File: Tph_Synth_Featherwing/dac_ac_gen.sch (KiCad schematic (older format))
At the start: 10 parts, among them U4 MCP4728

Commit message: Added BOM and upgraded to kicad 5.0
Signed-off-by: Tisham Dhar <whatnickd@gmail.com>
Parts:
- C13, C14, C15, C16, C17: manf# (none) -> GCM188L81H104KA57D
- R16, R17: manf# (none) -> RC0603FR-072K2L
- TP6, TP7: DNP (none) -> (none)
- U4: manf# (none) -> MCP4728-E/UN
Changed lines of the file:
@@
 EESchema Schematic File Version 4
-LIBS:Tph_Synth_Featherwing-cache
-EELAYER 26 0
+EELAYER 30 0
 EELAYER END
 $Descr A4 11693 8268
@@
 F 2 "Package_SO:MSOP-10_3x3mm_P0.5mm" H 4110 2770 50  0001 C CNN
 F 3 "http://ww1.microchip.com/downloads/en/DeviceDoc/22187E.pdf" H 4110 3620 50  0001 C CNN
+F 4 "MCP4728-E/UN" H 4110 3370 50  0001 C CNN "manf#"
 	1    4110 3370
 	1    0    0    -1
@@
 F 2 "Capacitor_SMD:C_0603_1608Metric" H 4380 3030 50  0001 C CNN
 F 3 "~" H 4380 3030 50  0001 C CNN
+F 4 "GCM188L81H104KA57D" H 4380 3030 50  0001 C CNN "manf#"
 	1    4380 3030
 	0    1    1    0
@@
 F 2 "Resistor_SMD:R_0603_1608Metric" H 3075 3135 50  0001 C CNN
 F 3 "~" H 3075 3135 50  0001 C CNN
+F 4 "RC0603FR-072K2L" H 3075 3135 50  0001 C CNN "manf#"
 	1    3075 3135
 	1    0    0    -1
@@
 F 2 "Resistor_SMD:R_0603_1608Metric" H 2785 3140 50  0001 C CNN
 F 3 "~" H 2785 3140 50  0001 C CNN
+F 4 "RC0603FR-072K2L" H 2785 3140 50  0001 C CNN "manf#"
 	1    2785 3140
 	1    0    0    -1
@@
 F 2 "TestPoint:TestPoint_Pad_D1.0mm" H 3710 3470 50  0001 C CNN
 F 3 "~" H 3710 3470 50  0001 C CNN
+F 4 " " H 3510 3470 50  0001 C CNN "DNP"
 	1    3510 3470
 	0    -1   -1   0
@@
 F 2 "TestPoint:TestPoint_Pad_D1.0mm" H 3710 3570 50  0001 C CNN
 F 3 "~" H 3710 3570 50  0001 C CNN
+F 4 " " H 3510 3570 50  0001 C CNN "DNP"
 	1    3510 3570
 	0    -1   -1   0
@@
 F 2 "Capacitor_SMD:C_0603_1608Metric" H 4725 3785 50  0001 C CNN
 F 3 "~" H 4725 3785 50  0001 C CNN
+F 4 "GCM188L81H104KA57D" H 4725 3785 50  0001 C CNN "manf#"
 	1    4725 3785
 	1    0    0    -1
@@
 F 2 "Capacitor_SMD:C_0603_1608Metric" H 4870 3785 50  0001 C CNN
 F 3 "~" H 4870 3785 50  0001 C CNN
+F 4 "GCM188L81H104KA57D" H 4870 3785 50  0001 C CNN "manf#"
 	1    4870 3785
 	1    0    0    -1
@@
 F 2 "Capacitor_SMD:C_0603_1608Metric" H 5015 3785 50  0001 C CNN
 F 3 "~" H 5015 3785 50  0001 C CNN
+F 4 "GCM188L81H104KA57D" H 5015 3785 50  0001 C CNN "manf#"
 	1    5015 3785
 	1    0    0    -1
@@
 F 2 "Capacitor_SMD:C_0603_1608Metric" H 5165 3785 50  0001 C CNN
 F 3 "~" H 5165 3785 50  0001 C CNN
+F 4 "GCM188L81H104KA57D" H 5165 3785 50  0001 C CNN "manf#"
 	1    5165 3785
 	1    0    0    -1

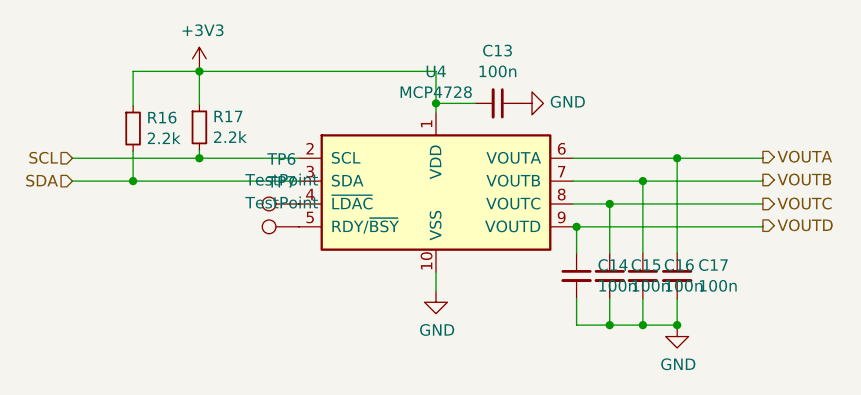
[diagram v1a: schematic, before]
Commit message: #1 and #2 add mising wiring
Signed-off-by: Tisham Dhar <whatnickd@gmail.com>
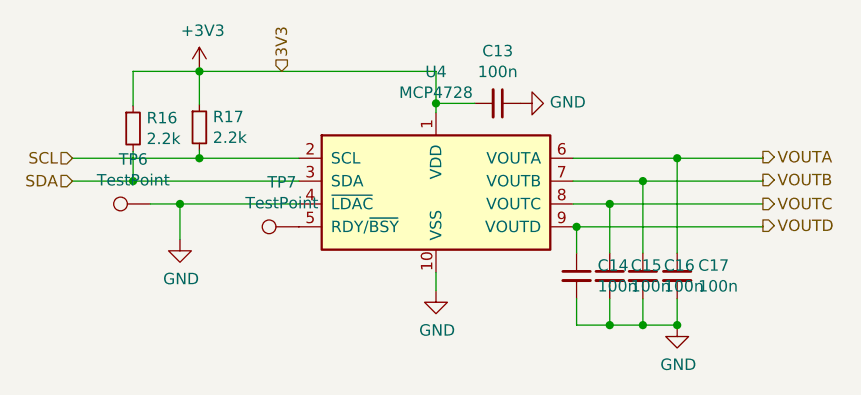
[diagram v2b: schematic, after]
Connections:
- net GND: now also TP6.1, U4.4 (~LDAC)
- net 3V3: now reaches C13.2, R16.1, R17.1, U4.1 (VDD)
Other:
- moved on the sheet: TP6
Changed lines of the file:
@@
 L Connector:TestPoint TP6
 U 1 1 5DECF0BD
-P 3510 3470
-F 0 "TP6" V 3705 3544 50  0000 C CNN
-F 1 "TestPoint" V 3614 3544 50  0000 C CNN
-F 2 "TestPoint:TestPoint_Pad_D1.0mm" H 3710 3470 50  0001 C CNN
-F 3 "~" H 3710 3470 50  0001 C CNN
-F 4 " " H 3510 3470 50  0001 C CNN "DNP"
-	1    3510 3470
+P 2860 3470
+F 0 "TP6" V 3055 3544 50  0000 C CNN
+F 1 "TestPoint" V 2964 3544 50  0000 C CNN
+F 2 "TestPoint:TestPoint_Pad_D1.0mm" H 3060 3470 50  0001 C CNN
+F 3 "~" H 3060 3470 50  0001 C CNN
+F 4 " " H 2860 3470 50  0001 C CNN "DNP"
+	1    2860 3470
 	0    -1   -1   0
 $EndComp
@@
 $EndComp
 Connection ~ 5165 4000
+$Comp
+L power:GND #PWR0101
+U 1 1 5E357714
+P 2990 3625
+F 0 "#PWR0101" H 2990 3375 50  0001 C CNN
+F 1 "GND" H 2995 3452 50  0000 C CNN
+F 2 "" H 2990 3625 50  0001 C CNN
+F 3 "" H 2990 3625 50  0001 C CNN
+	1    2990 3625
+	1    0    0    -1
+$EndComp
+Wire Wire Line
+	3510 3470 2990 3470
+Wire Wire Line
+	2990 3625 2990 3470
+Connection ~ 2990 3470
+Wire Wire Line
+	2990 3470 2860 3470
+Text HLabel 3435 2890 1    50   Input ~ 0
+3V3
 $EndSCHEMATC
